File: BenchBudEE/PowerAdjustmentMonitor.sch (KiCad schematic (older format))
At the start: 0 parts

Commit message: Power monitor module blocked out (needs tidying)
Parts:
- added JP? (x3): JUMPER, ~, symbol JUMPER
- added R? (x8): R, ~, symbol R
- added R? (x2): RVAR, ~, symbol RVAR
- added U? (x2): LM317, ~, symbol LM317
- added U? (x2): LM7805, ~, symbol LM7805
- added U? (x2): LM324, symbol LM324
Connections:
- net labels added: +12V, +3.3V, +5V, -12V, 3V3_MON, 5V_MON, AGND, FE_V+, FE_V-, GND, V+_ADJ, V+_ADJ_MON, V+_CUR_MON, V+_MON, V-_ADJ, V-_ADJ_MON, V-_CUR_MON, V-_MON
- wire segments 0 -> 78

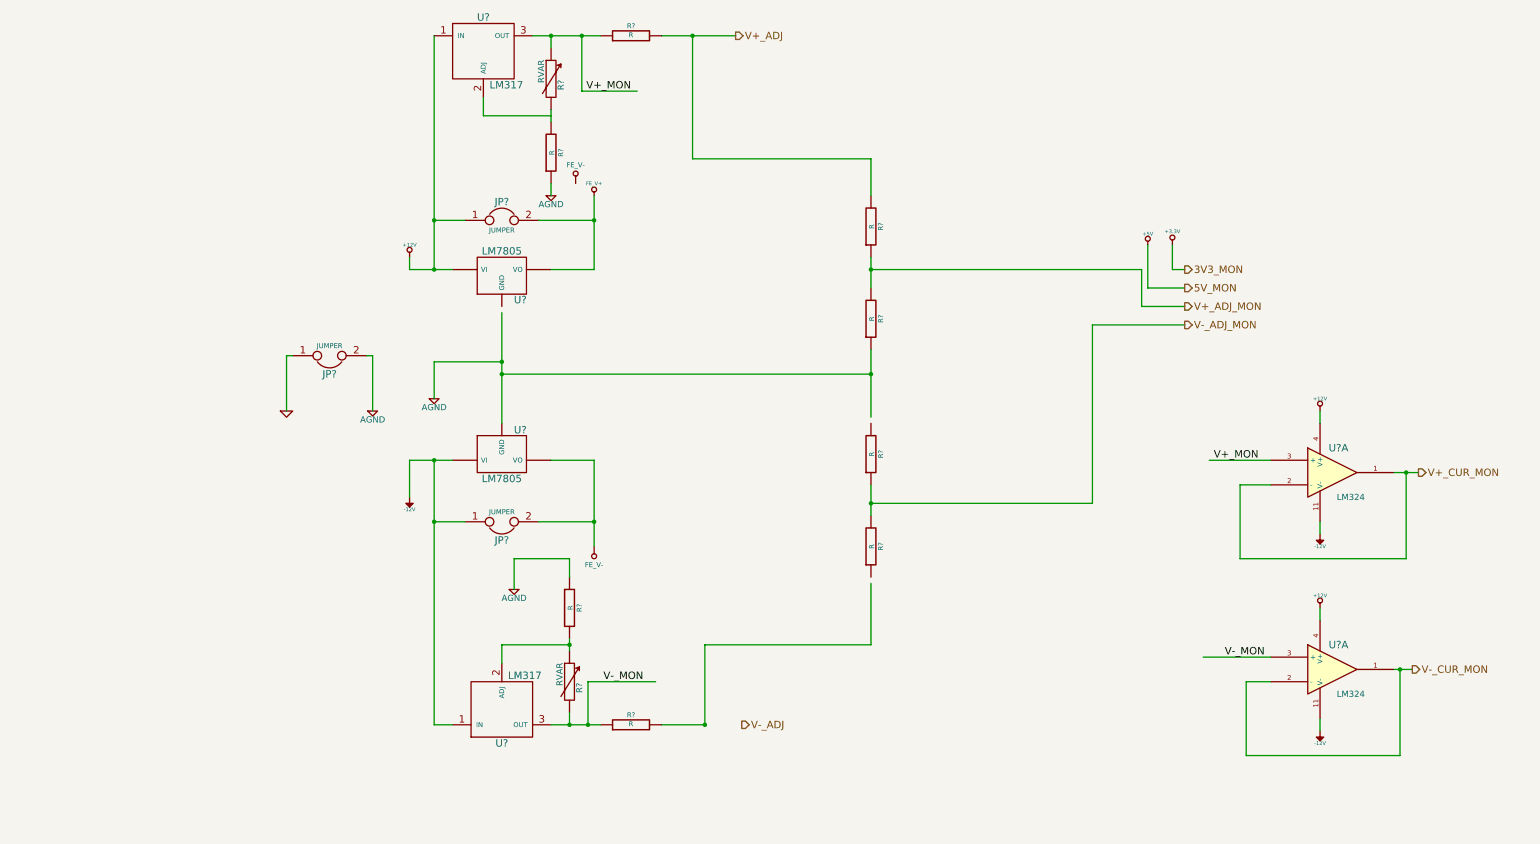
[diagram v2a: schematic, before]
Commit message: Parts added to relay module. Schematic tidied up.
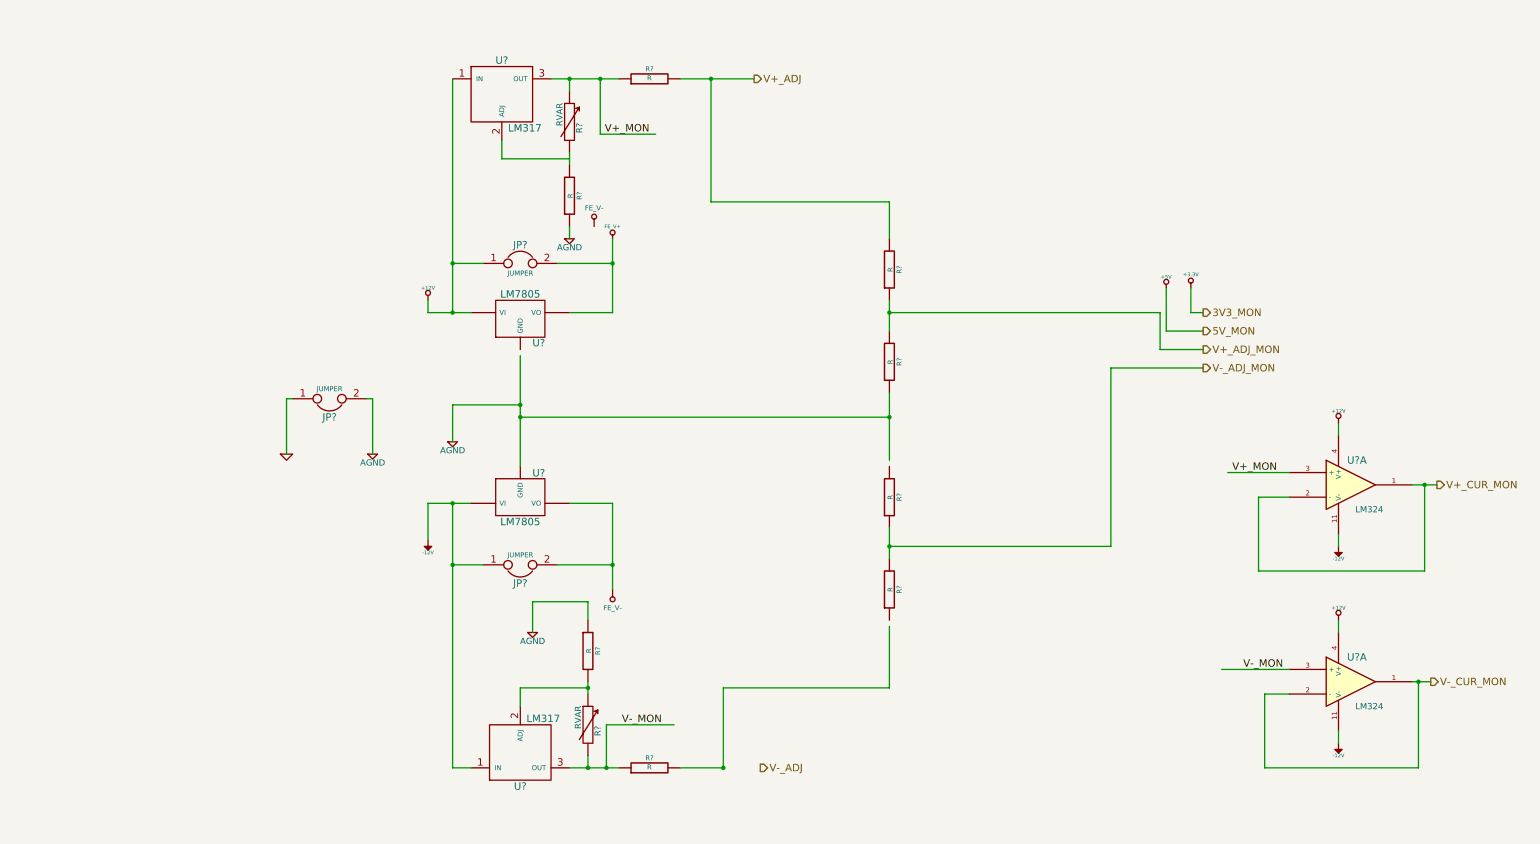
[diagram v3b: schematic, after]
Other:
- moved on the sheet: JP?, R?, U?, U?A

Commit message: Design rules specified for layout.
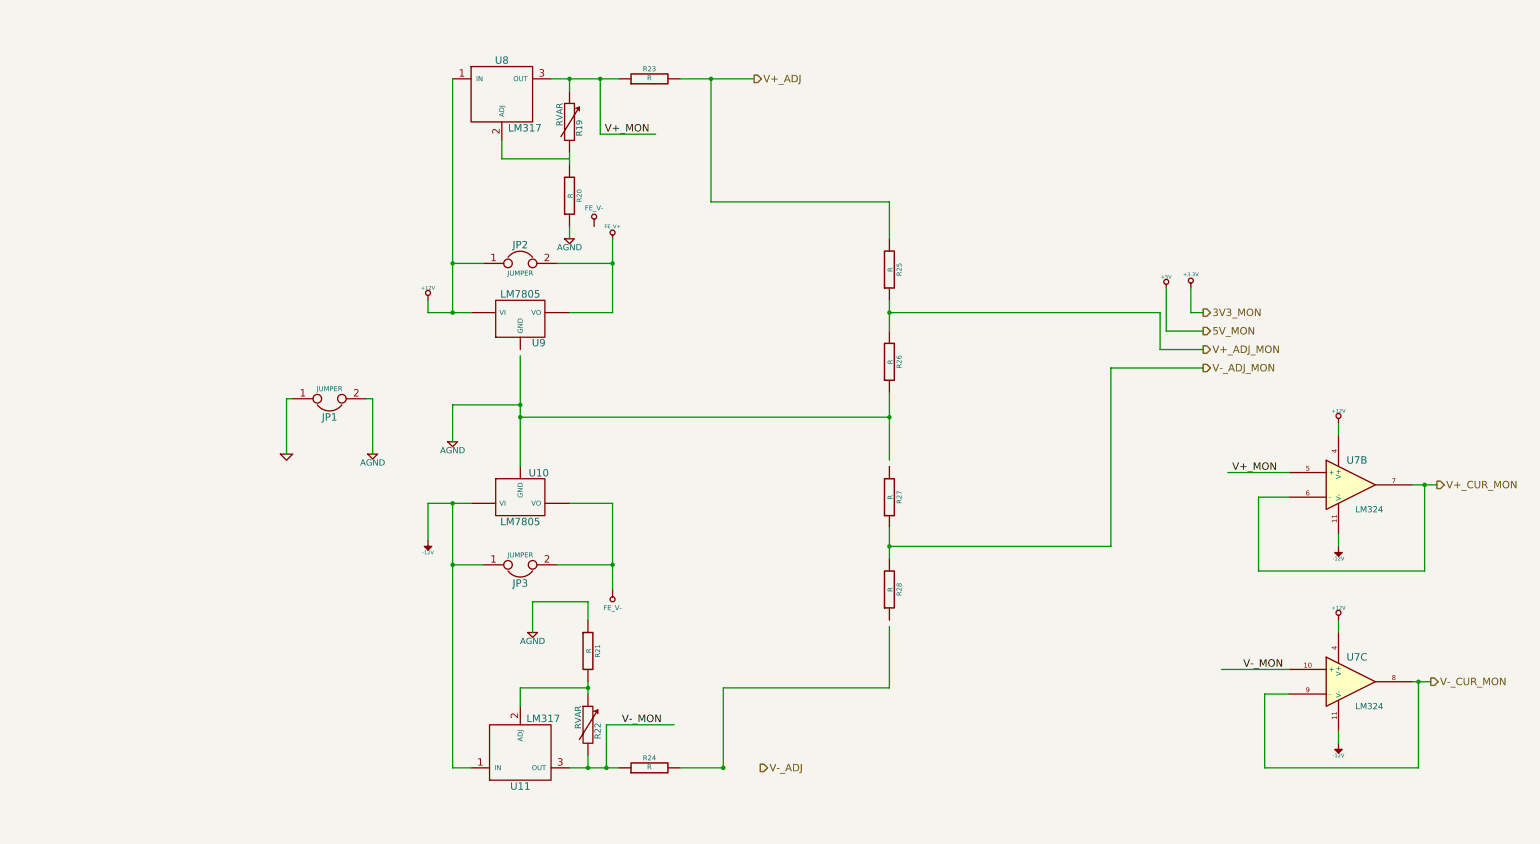
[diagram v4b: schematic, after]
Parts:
- gave numbers to parts that had none: 18
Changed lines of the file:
@@
 $EndDescr
 $Comp
-L +3.3V #PWR?
+L +3.3V #PWR49
 U 1 1 52F30EBD
 P 8050 2750
-F 0 "#PWR?" H 8050 2710 30  0001 C CNN
+F 0 "#PWR49" H 8050 2710 30  0001 C CNN
 F 1 "+3.3V" H 8050 2860 30  0000 C CNN
 F 2 "" H 8050 2750 60  0000 C CNN
@@
 $EndComp
 $Comp
-L +5V #PWR?
+L +5V #PWR48
 U 1 1 52F30EC3
 P 7850 2750
-F 0 "#PWR?" H 7850 2840 20  0001 C CNN
+F 0 "#PWR48" H 7850 2840 20  0001 C CNN
 F 1 "+5V" H 7850 2840 30  0000 C CNN
 F 2 "" H 7850 2750 60  0000 C CNN
@@
 $EndComp
 $Comp
-L +12V #PWR?
+L +12V #PWR40
 U 1 1 52F31364
 P 1850 2850
-F 0 "#PWR?" H 1850 2800 20  0001 C CNN
+F 0 "#PWR40" H 1850 2800 20  0001 C CNN
 F 1 "+12V" H 1850 2950 30  0000 C CNN
 F 2 "" H 1850 2850 60  0000 C CNN
@@
 $EndComp
 $Comp
-L -12V #PWR?
+L -12V #PWR41
 U 1 1 52F31373
 P 1850 4800
-F 0 "#PWR?" H 1850 4930 20  0001 C CNN
+F 0 "#PWR41" H 1850 4930 20  0001 C CNN
 F 1 "-12V" H 1850 4900 30  0000 C CNN
 F 2 "" H 1850 4800 60  0000 C CNN
@@
 $EndComp
 $Comp
-L LM317 U?
+L LM317 U11
 U 1 1 52F3155C
 P 2600 6500
-F 0 "U?" H 2600 6800 60  0000 C CNN
+F 0 "U11" H 2600 6800 60  0000 C CNN
 F 1 "LM317" H 2650 6250 60  0000 L CNN
 F 2 "~" H 2600 6500 60  0000 C CNN
@@
 $EndComp
 $Comp
-L JUMPER JP?
+L JUMPER JP3
 U 1 1 52F31575
 P 2600 5000
-F 0 "JP?" H 2600 5150 60  0000 C CNN
+F 0 "JP3" H 2600 5150 60  0000 C CNN
 F 1 "JUMPER" H 2600 4920 40  0000 C CNN
 F 2 "~" H 2600 5000 60  0000 C CNN
@@
 $EndComp
 $Comp
-L JUMPER JP?
+L JUMPER JP2
 U 1 1 52F31582
 P 2600 2550
-F 0 "JP?" H 2600 2700 60  0000 C CNN
+F 0 "JP2" H 2600 2700 60  0000 C CNN
 F 1 "JUMPER" H 2600 2470 40  0000 C CNN
 F 2 "~" H 2600 2550 60  0000 C CNN
@@
 $EndComp
 $Comp
-L JUMPER JP?
+L JUMPER JP1
 U 1 1 52F315DF
 P 1050 3650
-F 0 "JP?" H 1050 3800 60  0000 C CNN
+F 0 "JP1" H 1050 3800 60  0000 C CNN
 F 1 "JUMPER" H 1050 3570 40  0000 C CNN
 F 2 "~" H 1050 3650 60  0000 C CNN
@@
 $EndComp
 $Comp
-L GND #PWR?
+L GND #PWR38
 U 1 1 52F315E7
 P 700 4100
-F 0 "#PWR?" H 700 4100 30  0001 C CNN
+F 0 "#PWR38" H 700 4100 30  0001 C CNN
 F 1 "GND" H 700 4030 30  0001 C CNN
 F 2 "" H 700 4100 60  0000 C CNN
@@
 $EndComp
 $Comp
-L AGND #PWR?
+L AGND #PWR39
 U 1 1 52F315F6
 P 1400 4100
-F 0 "#PWR?" H 1400 4100 40  0001 C CNN
+F 0 "#PWR39" H 1400 4100 40  0001 C CNN
 F 1 "AGND" H 1400 4030 50  0000 C CNN
 F 2 "" H 1400 4100 60  0000 C CNN
@@
 $EndComp
 $Comp
-L FE_V+ #PWR?
+L FE_V+ #PWR46
 U 1 1 52F316C5
 P 3350 2350
-F 0 "#PWR?" H 3350 2450 30  0001 C CNN
+F 0 "#PWR46" H 3350 2450 30  0001 C CNN
 F 1 "FE_V+" H 3350 2450 30  0000 C CNN
 F 2 "" H 3350 2350 60  0000 C CNN
@@
 $EndComp
 $Comp
-L FE_V- #PWR?
+L FE_V- #PWR47
 U 1 1 52F316D4
 P 3350 5200
-F 0 "#PWR?" H 3350 5400 40  0001 C CNN
+F 0 "#PWR47" H 3350 5400 40  0001 C CNN
 F 1 "FE_V-" H 3350 5350 40  0000 C CNN
 F 2 "" H 3350 5200 60  0000 C CNN
@@
 $EndComp
 $Comp
-L AGND #PWR?
+L AGND #PWR42
 U 1 1 52F31737
 P 2050 4000
-F 0 "#PWR?" H 2050 4000 40  0001 C CNN
+F 0 "#PWR42" H 2050 4000 40  0001 C CNN
 F 1 "AGND" H 2050 3930 50  0000 C CNN
 F 2 "" H 2050 4000 60  0000 C CNN
@@
 $EndComp
 $Comp
-L LM7805 U?
+L LM7805 U9
 U 1 1 52F3175A
 P 2600 3000
-F 0 "U?" H 2750 2804 60  0000 C CNN
+F 0 "U9" H 2750 2804 60  0000 C CNN
 F 1 "LM7805" H 2600 3200 60  0000 C CNN
 F 2 "~" H 2600 3000 60  0000 C CNN
@@
 $EndComp
 $Comp
-L LM7805 U?
+L LM7805 U10
 U 1 1 52F31767
 P 2600 4450
-F 0 "U?" H 2750 4254 60  0000 C CNN
+F 0 "U10" H 2750 4254 60  0000 C CNN
 F 1 "LM7805" H 2600 4650 60  0000 C CNN
 F 2 "~" H 2600 4450 60  0000 C CNN
@@
 $EndComp
 $Comp
-L R R?
+L R R21
 U 1 1 52F31835
 P 3150 5700
-F 0 "R?" V 3230 5700 40  0000 C CNN
+F 0 "R21" V 3230 5700 40  0000 C CNN
 F 1 "R" V 3157 5701 40  0000 C CNN
 F 2 "~" V 3080 5700 30  0000 C CNN
@@
 $EndComp
 $Comp
-L LM317 U?
+L LM317 U8
 U 1 1 52F318EF
 P 2450 1200
-F 0 "U?" H 2450 1500 60  0000 C CNN
+F 0 "U8" H 2450 1500 60  0000 C CNN
 F 1 "LM317" H 2500 950 60  0000 L CNN
 F 2 "~" H 2450 1200 60  0000 C CNN
@@
 $EndComp
 $Comp
-L FE_V- #PWR?
+L FE_V- #PWR45
 U 1 1 52F318F5
 P 3200 2250
-F 0 "#PWR?" H 3200 2450 40  0001 C CNN
+F 0 "#PWR45" H 3200 2450 40  0001 C CNN
 F 1 "FE_V-" H 3200 2400 40  0000 C CNN
 F 2 "" H 3200 2250 60  0000 C CNN
@@
 $EndComp
 $Comp
-L R R?
+L R R20
 U 1 1 52F31901
 P 3000 2000
-F 0 "R?" V 3080 2000 40  0000 C CNN
+F 0 "R20" V 3080 2000 40  0000 C CNN
 F 1 "R" V 3007 2001 40  0000 C CNN
 F 2 "~" V 2930 2000 30  0000 C CNN
@@
 $EndComp
 $Comp
-L AGND #PWR?
+L AGND #PWR43
 U 1 1 52F3195F
 P 2700 5550
-F 0 "#PWR?" H 2700 5550 40  0001 C CNN
+F 0 "#PWR43" H 2700 5550 40  0001 C CNN
 F 1 "AGND" H 2700 5480 50  0000 C CNN
 F 2 "" H 2700 5550 60  0000 C CNN
@@
 $EndComp
 $Comp
-L AGND #PWR?
+L AGND #PWR44
 U 1 1 52F319EB
 P 3000 2350
-F 0 "#PWR?" H 3000 2350 40  0001 C CNN
+F 0 "#PWR44" H 3000 2350 40  0001 C CNN
 F 1 "AGND" H 3000 2280 50  0000 C CNN
 F 2 "" H 3000 2350 60  0000 C CNN
@@
 V-_CUR_MON
 $Comp
-L R R?
+L R R25
 U 1 1 52F31BDF
 P 5600 2600
-F 0 "R?" V 5680 2600 40  0000 C CNN
+F 0 "R25" V 5680 2600 40  0000 C CNN
 F 1 "R" V 5607 2601 40  0000 C CNN
 F 2 "~" V 5530 2600 30  0000 C CNN
@@
 $EndComp
 $Comp
-L R R?
+L R R26
 U 1 1 52F31BE5
 P 5600 3350
-F 0 "R?" V 5680 3350 40  0000 C CNN
+F 0 "R26" V 5680 3350 40  0000 C CNN
 F 1 "R" V 5607 3351 40  0000 C CNN
 F 2 "~" V 5530 3350 30  0000 C CNN
@@
 $EndComp
 $Comp
-L R R?
+L R R27
 U 1 1 52F31C82
 P 5600 4450
-F 0 "R?" V 5680 4450 40  0000 C CNN
+F 0 "R27" V 5680 4450 40  0000 C CNN
 F 1 "R" V 5607 4451 40  0000 C CNN
 F 2 "~" V 5530 4450 30  0000 C CNN
@@
 $EndComp
 $Comp
-L R R?
+L R R28
 U 1 1 52F31C88
 P 5600 5200
-F 0 "R?" V 5680 5200 40  0000 C CNN
+F 0 "R28" V 5680 5200 40  0000 C CNN
 F 1 "R" V 5607 5201 40  0000 C CNN
 F 2 "~" V 5530 5200 30  0000 C CNN
@@
 $EndComp
 $Comp
-L R R?
+L R R24
 U 1 1 52F31E91
 P 3650 6650
-F 0 "R?" V 3730 6650 40  0000 C CNN
+F 0 "R24" V 3730 6650 40  0000 C CNN
 F 1 "R" V 3657 6651 40  0000 C CNN
 F 2 "~" V 3580 6650 30  0000 C CNN
@@
 $EndComp
 $Comp
-L R R?
+L R R23
 U 1 1 52F31F87
 P 3650 1050
-F 0 "R?" V 3730 1050 40  0000 C CNN
+F 0 "R23" V 3730 1050 40  0000 C CNN
 F 1 "R" V 3657 1051 40  0000 C CNN
 F 2 "~" V 3580 1050 30  0000 C CNN
@@
 V+_MON
 $Comp
-L LM324 U?
-U 1 1 52F320BE
+L LM324 U7
+U 3 1 52F320BE
 P 9350 5950
-F 0 "U?" H 9400 6150 60  0000 C CNN
+F 0 "U7" H 9400 6150 60  0000 C CNN
 F 1 "LM324" H 9500 5750 50  0000 C CNN
 F 2 "" H 9350 5950 60  0000 C CNN
 F 3 "" H 9350 5950 60  0000 C CNN
-	1    9350 5950
-	1    0    0    -1
-$EndComp
-$Comp
-L +12V #PWR?
+	3    9350 5950
+	1    0    0    -1
+$EndComp
+$Comp
+L +12V #PWR52
 U 1 1 52F320CB
 P 9250 5450
-F 0 "#PWR?" H 9250 5400 20  0001 C CNN
+F 0 "#PWR52" H 9250 5400 20  0001 C CNN
 F 1 "+12V" H 9250 5550 30  0000 C CNN
 F 2 "" H 9250 5450 60  0000 C CNN
@@
 $EndComp
 $Comp
-L -12V #PWR?
+L -12V #PWR53
 U 1 1 52F320D1
 P 9250 6450
-F 0 "#PWR?" H 9250 6580 20  0001 C CNN
+F 0 "#PWR53" H 9250 6580 20  0001 C CNN
 F 1 "-12V" H 9250 6550 30  0000 C CNN
 F 2 "" H 9250 6450 60  0000 C CNN
@@
 $EndComp
 $Comp
-L LM324 U?
-U 1 1 52F3217A
+L LM324 U7
+U 2 1 52F3217A
 P 9350 4350
-F 0 "U?" H 9400 4550 60  0000 C CNN
+F 0 "U7" H 9400 4550 60  0000 C CNN
 F 1 "LM324" H 9500 4150 50  0000 C CNN
 F 2 "" H 9350 4350 60  0000 C CNN
 F 3 "" H 9350 4350 60  0000 C CNN
-	1    9350 4350
-	1    0    0    -1
-$EndComp
-$Comp
-L +12V #PWR?
+	2    9350 4350
+	1    0    0    -1
+$EndComp
+$Comp
+L +12V #PWR50
 U 1 1 52F32180
 P 9250 3850
-F 0 "#PWR?" H 9250 3800 20  0001 C CNN
+F 0 "#PWR50" H 9250 3800 20  0001 C CNN
 F 1 "+12V" H 9250 3950 30  0000 C CNN
 F 2 "" H 9250 3850 60  0000 C CNN
@@
 $EndComp
 $Comp
-L -12V #PWR?
+L -12V #PWR51
 U 1 1 52F32186
 P 9250 4850
-F 0 "#PWR?" H 9250 4980 20  0001 C CNN
+F 0 "#PWR51" H 9250 4980 20  0001 C CNN
 F 1 "-12V" H 9250 4950 30  0000 C CNN
 F 2 "" H 9250 4850 60  0000 C CNN
@@
 	2700 5300 2700 5550
 $Comp
-L RVAR R?
+L RVAR R22
 U 1 1 52F324F0
 P 3150 6300
-F 0 "R?" V 3230 6250 50  0000 C CNN
+F 0 "R22" V 3230 6250 50  0000 C CNN
 F 1 "RVAR" V 3070 6360 50  0000 C CNN
 F 2 "~" H 3150 6300 60  0000 C CNN
@@
 	3150 6050 3150 5950
 $Comp
-L RVAR R?
+L RVAR R19
 U 1 1 52F325C3
 P 3000 1400
-F 0 "R?" V 3080 1350 50  0000 C CNN
+F 0 "R19" V 3080 1350 50  0000 C CNN
 F 1 "RVAR" V 2920 1460 50  0000 C CNN
 F 2 "~" H 3000 1400 60  0000 C CNN
